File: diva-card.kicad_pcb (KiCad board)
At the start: 2 copper layers, 85.4 x 53.7 mm, 88 parts, among them J1 Conn_02x05_Odd_Even, J2 USB_C_Receptacle_USB2.0, J3 Conn_02x21_Odd_Even, SW1 SW_Push, SW2 SW_Push, U1 AP2112K-3.3, U2 ATECC608A-SSHDA, U3 W25Q128JVS, U4 RP2040, Y1 Crystal_GND24

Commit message: Adding test gerber and bom
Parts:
- D1: value RED -> EMERALD
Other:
- board text added: "0"
- board text added: "40"
- board text added: "RGB Matrix"
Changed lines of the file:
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@@
     (property "Sheetfile" "connectors.kicad_sch")
     (property "Sheetname" "connectors")
+    (attr exclude_from_bom)
     (fp_text reference "J3" (at 0 -26.9 unlocked) (layer "F.Fab")
       (effects (font (size 1 1) (thickness 0.15)))
@@
       (effects (font (size 1 1) (thickness 0.15)))
     )
-    (fp_text value "RED" (at 0 1.17) (layer "F.Fab")
+    (fp_text value "EMERALD" (at 0 1.17) (layer "F.Fab")
       (effects (font (size 1 1) (thickness 0.15)))
     )
@@
     (fp_line (start -2.5 -3.5) (end 3.5 -3.5) (layer "F.Fab") (width 0.1))
     (fp_line (start -3.5 -2.5) (end -2.5 -3.5) (layer "F.Fab") (width 0.1))
-    (pad "" smd roundrect (at -0.6375 0.6375 180) (size 1.084435 1.084435) (layers "F.Paste") (roundrect_rratio 0.230535))
-    (pad "" smd roundrect (at 0.6375 -0.6375 180) (size 1.084435 1.084435) (layers "F.Paste") (roundrect_rratio 0.230535))
-    (pad "" smd roundrect (at -0.6375 -0.6375 180) (size 1.084435 1.084435) (layers "F.Paste") (roundrect_rratio 0.230535))
-    (pad "" smd roundrect (at 0.6375 0.6375 180) (size 1.084435 1.084435) (layers "F.Paste") (roundrect_rratio 0.230535))
+    (pad "" smd roundrect (at -0.6375 0.6375 180) (size 1.084435 1.084435) (layers "F.Paste") (roundrect_rratio 0.2305347946))
+    (pad "" smd roundrect (at 0.6375 -0.6375 180) (size 1.084435 1.084435) (layers "F.Paste") (roundrect_rratio 0.2305347946))
+    (pad "" smd roundrect (at -0.6375 -0.6375 180) (size 1.084435 1.084435) (layers "F.Paste") (roundrect_rratio 0.2305347946))
+    (pad "" smd roundrect (at 0.6375 0.6375 180) (size 1.084435 1.084435) (layers "F.Paste") (roundrect_rratio 0.2305347946))
     (pad "1" smd roundrect (at -3.4375 -2.6 180) (size 0.875 0.2) (layers "F.Cu" "F.Paste" "F.Mask") (roundrect_rratio 0.25)
       (net 2 "+3V3") (pinfunction "IOVDD") (pintype "power_in"))
@@
     (property "Sheetfile" "connectors.kicad_sch")
     (property "Sheetname" "connectors")
-    (attr exclude_from_pos_files)
+    (attr exclude_from_pos_files exclude_from_bom)
     (fp_text reference "J1" (at 0 -2.6) (layer "F.Fab")
       (effects (font (size 1 1) (thickness 0.15)))
@@
     (property "Sheetfile" "peripherals.kicad_sch")
     (property "Sheetname" "peripherals")
-    (attr smd)
+    (attr smd exclude_from_bom)
     (fp_text reference "R3" (at -0.02 1.65 180) (layer "F.SilkS")
       (effects (font (size 1 1) (thickness 0.15)))
@@
   (gr_line (start 99.744 97.13) (end 100.76 96.114) (layer "F.SilkS") (width 0.15))
   (gr_line (start 95.32 97.13) (end 99.744 97.13) (layer "F.SilkS") (width 0.15))
+  (gr_line (start 109.45 105.333) (end 109.45 110.8) (layer "F.SilkS") (width 0.15))
   (gr_line (start 72.459 90.209) (end 73.475 91.225) (layer "F.SilkS") (width 0.15))
   (gr_line (start 78.876 97.875) (end 77.86 98.891) (layer "F.SilkS") (width 0.15))
@@
   (gr_line (start 137.057 81.274) (end 136.041 82.29) (layer "F.SilkS") (width 0.15))
   (gr_line (start 137.057 98.842) (end 136.041 99.858) (layer "F.SilkS") (width 0.15))
+  (gr_line (start 110.466 104.317) (end 109.45 105.333) (layer "F.SilkS") (width 0.15))
   (gr_line (start 86.534 78.534) (end 80.143 78.534) (layer "F.SilkS") (width 0.15))
   (gr_line (start 136.041 88.386) (end 136.041 91.434) (layer "F.SilkS") (width 0.15))
@@
   (gr_line (start 102.884 100.284) (end 103.9 101.3) (layer "F.SilkS") (width 0.15))
   (gr_line (start 136.041 82.29) (end 136.041 85.338) (layer "F.SilkS") (width 0.15))
-  (gr_line (start 107.232 74.692) (end 102.808 74.692) (layer "F.SilkS") (width 0.15))
+  (gr_line (start 109.049 74.8) (end 104.625 74.8) (layer "F.SilkS") (width 0.15))
   (gr_line (start 136.041 99.858) (end 136.041 102.906) (layer "F.SilkS") (width 0.15))
   (gr_line (start 136.041 111.754) (end 137.057 112.77) (layer "F.SilkS") (width 0.15))
@@
   (gr_line (start 83.3 97.875) (end 78.876 97.875) (layer "F.SilkS") (width 0.15))
   (gr_line (start 137.057 62.478) (end 136.041 63.494) (layer "F.SilkS") (width 0.15))
-  (gr_line (start 102.808 74.692) (end 101.792 75.708) (layer "F.SilkS") (width 0.15))
+  (gr_line (start 104.625 74.8) (end 103.609 75.816) (layer "F.SilkS") (width 0.15))
   (gr_line (start 72.459 88.084) (end 72.459 90.209) (layer "F.SilkS") (width 0.15))
   (gr_line locked (start 63.6 113.65) (end 63.6 61.35) (layer "Edge.Cuts") (width 0.1))
@@
     (effects (font (size 1 1) (thickness 0.15)))
   )
+  (gr_text "40" (at 128.025 69.875 90) (layer "F.SilkS")
+    (effects (font (size 1 1) (thickness 0.15)))
+  )
   (gr_text "SWD" (at 69.8 62.95) (layer "F.SilkS")
     (effects (font (size 1 1) (thickness 0.15)))
@@
     (effects (font (size 1 1) (thickness 0.15)))
   )
+  (gr_text "0" (at 109.85 102.375 90) (layer "F.SilkS")
+    (effects (font (size 1 1) (thickness 0.15)))
+  )
   (gr_text "V1.0" (at 70.5612 97.8408 90) (layer "F.SilkS")
     (effects (font (size 1 1) (thickness 0.25)))
@@
     (effects (font (size 1 1) (thickness 0.15)))
   )
-  (gr_text "Crypto" (at 105.04 73.66) (layer "F.SilkS")
+  (gr_text "Crypto" (at 106.857 73.768) (layer "F.SilkS")
     (effects (font (size 1 1) (thickness 0.15)))
   )
@@
     (effects (font (size 1 1) (thickness 0.15)))
   )
+  (gr_text "RGB Matrix" (at 108.75 108.175 90) (layer "F.SilkS")
+    (effects (font (size 1 1) (thickness 0.15)))
+  )
   (gr_text "DIVA CARD" (at 68.5612 97.8408 90) (layer "F.SilkS")
     (effects (font (size 1 1) (thickness 0.25)))
   )
-  (segment (start 92.5276 71.1876) (end 92.47 71.13) (width 0.5) (layer "F.Cu") (net 1))
   (segment (start 97.73 87.11) (end 98.62 87.11) (width 0.5) (layer "F.Cu") (net 1))
   (segment (start 120.393 104.768) (end 121.299 104.768) (width 0.3) (layer "F.Cu") (net 1))
@@
   (segment (start 114.963001 96.620242) (end 114.963001 96.018001) (width 0.3) (layer "F.Cu") (net 1))
   (segment (start 125.463001 91.977385) (end 125.463001 91.368001) (width 0.3) (layer "F.Cu") (net 1))
-  (segment (start 93.916 71.1876) (end 92.5276 71.1876) (width 0.5) (layer "F.Cu") (net 1))
   (segment (start 111.463 91.977385) (end 111.463 93.068) (width 0.3) (layer "F.Cu") (net 1))
   (segment (start 86 90.25) (end 86 88.095) (width 0.5) (layer "F.Cu") (net 1))
@@
   (segment (start 114.963001 101.2631) (end 114.963001 100.668001) (width 0.3) (layer "F.Cu") (net 1))
   (segment (start 79.3496 99.2704) (end 79.35 99.27) (width 0.5) (layer "F.Cu") (net 1))
+  (segment (start 92.475 71.2) (end 92.4874 71.1876) (width 0.5) (layer "F.Cu") (net 1))
   (segment (start 121.963001 87.334528) (end 121.963001 86.668501) (width 0.3) (layer "F.Cu") (net 1))
   (segment (start 118.463001 101.2631) (end 118.463001 100.668001) (width 0.3) (layer "F.Cu") (net 1))
@@
   (segment (start 125.463001 86.668001) (end 124.863 86.068) (width 0.3) (layer "F.Cu") (net 1))
   (segment (start 118.463001 72.783687) (end 117.872859 72.193545) (width 0.3) (layer "F.Cu") (net 1))
+  (segment (start 92.4874 71.1876) (end 93.916 71.1876) (width 0.5) (layer "F.Cu") (net 1))
   (segment (start 111.399976 97.704976) (end 111.413 97.718) (width 0.3) (layer "F.Cu") (net 1))
   (segment (start 114.963001 68.7631) (end 114.963 69.868) (width 0.3) (layer "F.Cu") (net 1))
@@
   (via (at 97.59 72.87) (size 0.7) (drill 0.3) (layers "F.Cu" "B.Cu") (net 1))
   (via (at 71.055659 67.4626) (size 0.7) (drill 0.3) (layers "F.Cu" "B.Cu") (net 1))
-  (via (at 92.47 71.13) (size 0.7) (drill 0.3) (layers "F.Cu" "B.Cu") (net 1))
+  (via (at 92.475 71.2) (size 0.7) (drill 0.3) (layers "F.Cu" "B.Cu") (net 1))
   (via (at 114.372859 86.093545) (size 0.7) (drill 0.3) (layers "F.Cu" "B.Cu") (net 1))
   (via (at 117.863 81.518) (size 0.7) (drill 0.3) (layers "F.Cu" "B.Cu") (net 1))

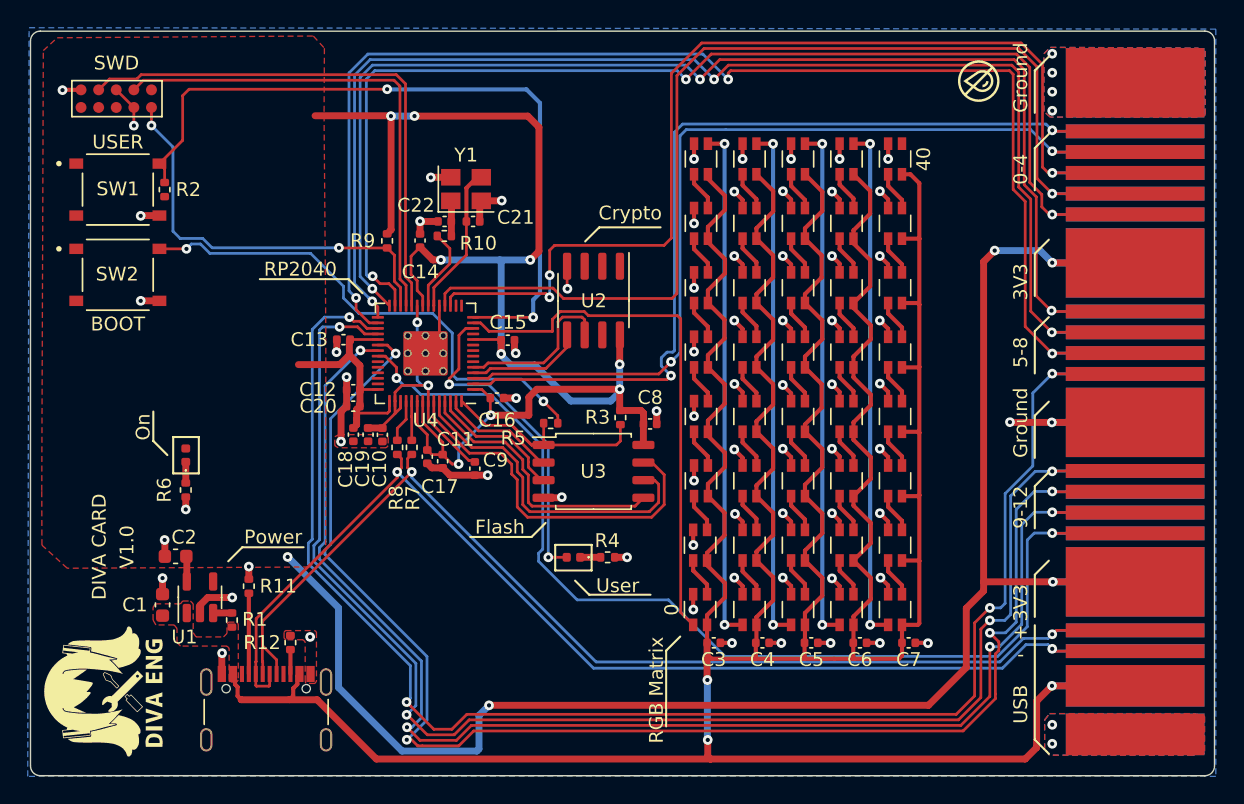
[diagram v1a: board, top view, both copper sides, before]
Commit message: updating footprints to udfn
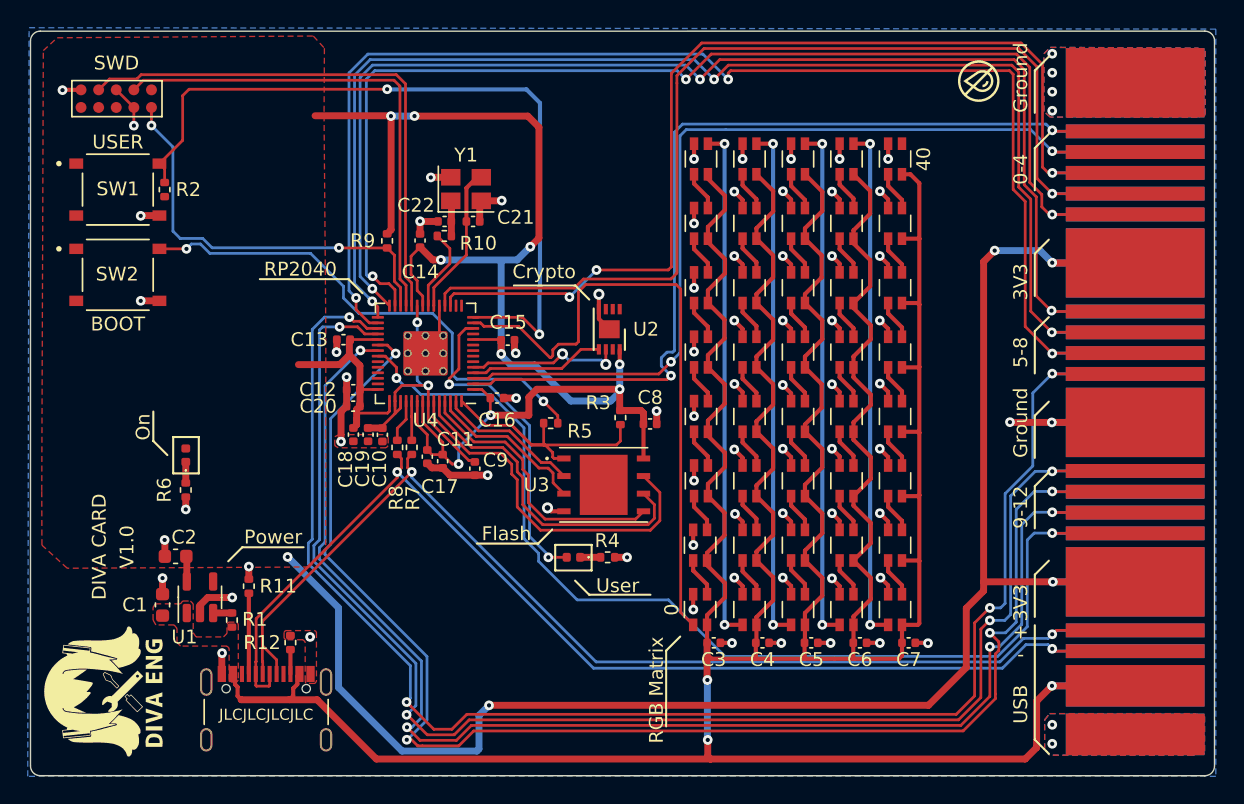
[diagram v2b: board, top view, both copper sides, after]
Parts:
- R5: value 1k -> 10k
- U2: value ATECC608A-SSHDA -> ATECC608A-MAHDA; footprint Package_SO:SOIC-8_3.9x4.9mm_P1.27mm -> Package_DFN_QFN:DFN-8-1EP_3x2mm_P0.5mm_EP1.3x1.5mm
- U3: value W25Q128JVS -> W25Q128XXX; footprint Package_SO:SOIC-8_5.23x5.23mm_P1.27mm -> Diva-Card:W25Q128JVPIQ TR
- moved U2 2.36 mm to (105.3, 82.2)
- moved U3 1.22 mm to (104.9, 93.4)
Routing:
- net /LED_DI: track 39.0 -> 45.3 mm
- net /microcontroller/~{QSPI_CS}: track 18.5 -> 20.6 mm
- net /~{USER_SW0}: track 53.5 -> 55.5 mm
- net /microcontroller/QSPI_SIO1: track 8.47 -> 10.3 mm
- net /microcontroller/QSPI_SIO2: track 9.90 -> 11.8 mm
- net /connectors/USER_IO_3: track 82.8 -> 81.4 mm
- net /I2C0_SDA: track 8.43 -> 9.77 mm
- net GND: track 114.9 -> 116.1 mm
- net /connectors/USER_IO_2: track 81.0 -> 80.2 mm
- net +3V3: track 252.1 -> 251.5 mm
- net /I2C0_SCL: track 11.9 -> 11.4 mm, vias 0 -> 2
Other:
- board text added: "JLCJLCJLCJLC"

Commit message: Adding schematic pdf
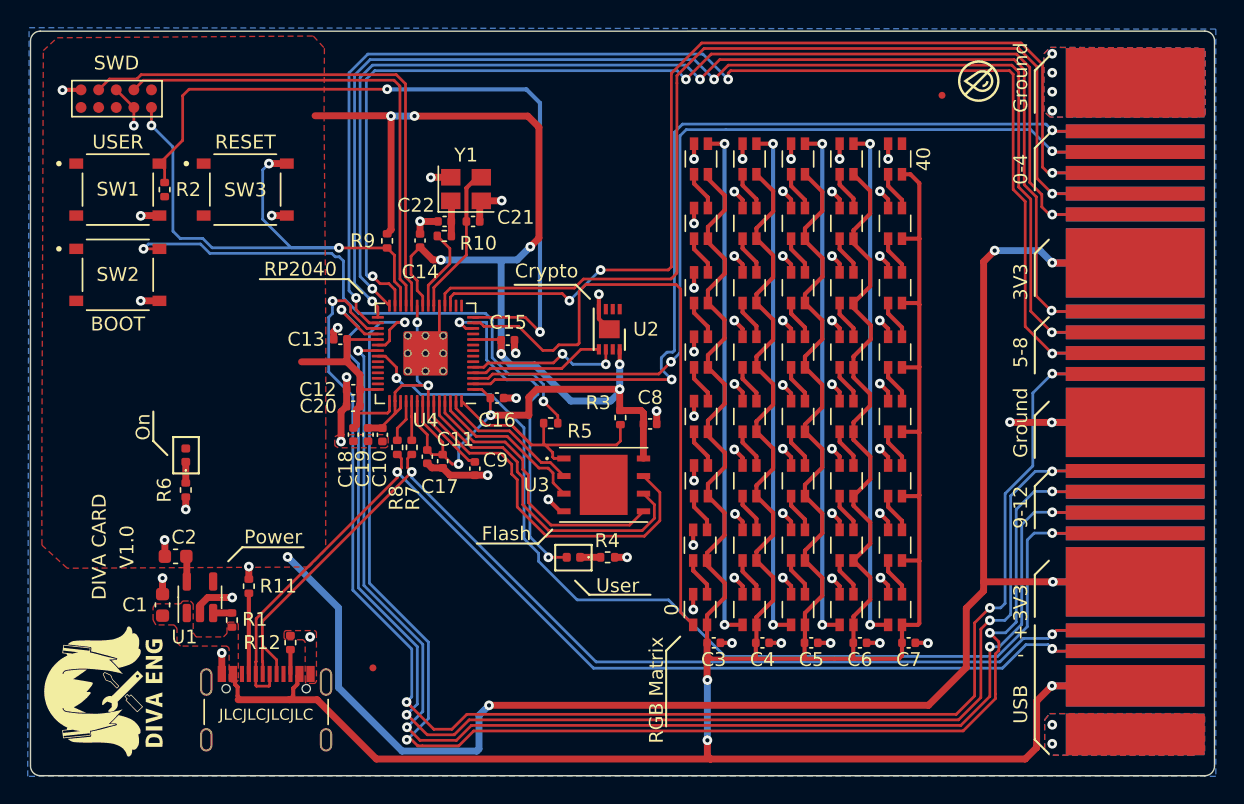
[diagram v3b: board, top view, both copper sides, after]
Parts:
- added FID1: Fiducial, Fiducial:Fiducial_0.5mm_Mask1mm, F.Cu at (88.3, 106.6)
- added FID2: Fiducial, Fiducial:Fiducial_0.5mm_Mask1mm, F.Cu at (129.3, 65.3)
- added SW3: RESET, Diva-Card:SW_TS-1187A-B-A-B, F.Cu at (79.1, 72.1)
- C21, C22: value 22p -> 33p
- R5: value 10k -> 1k
- SW1: value SW_Push -> USER
- SW2: value SW_Push -> BOOTSEL
- Y1: value Crystal_GND24 -> X322512MSB4SI
- moved C13 0.23 mm to (86.0, 82.9)
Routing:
- net /connectors/~{RESET}: track 30.1 -> 41.9 mm, vias 2 -> 3
- net /peripherals/~{USB_BOOT}: track 36.8 -> 40.7 mm
- net /connectors/USER_IO_10: track 110.0 -> 112.5 mm
- net /connectors/USER_IO_11: track 105.4 -> 103.0 mm
- net GND: track 116.1 -> 117.4 mm, vias 77 -> 78
- net /USER_LED: track 23.5 -> 24.8 mm
- net /microcontroller/~{QSPI_CS}: track 20.6 -> 19.6 mm
- net /LED_DI: track 45.3 -> 44.7 mm
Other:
- board text added: "RESET"

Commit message: design flaw fix
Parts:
- added C23: 1u, Capacitor_SMD:C_0402_1005Metric, F.Cu at (82.5, 72.0)
- added C24: 1u, Capacitor_SMD:C_0402_1005Metric, F.Cu at (101.8, 82.3)
- added C25: 1u, Capacitor_SMD:C_0402_1005Metric, F.Cu at (104.5, 89.0)
- R10: value 1k -> DNF
- R3: value DNF -> 10k
- moved FID1 4.17 mm to (88.6, 110.7)
- moved FID2 0.06 mm to (129.3, 65.3)
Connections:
- J3 pad 35: /connectors/USB_D+ -> unconnected-(J3-Pad35)
- J3 pad 36: /connectors/USB_D+ -> unconnected-(J3-Pad36)
- J3 pad 37: /connectors/USB_D- -> unconnected-(J3-Pad37)
- J3 pad 38: /connectors/USB_D- -> unconnected-(J3-Pad38)
- U4 pad 44: +1V1 -> +3V3
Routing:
- net +3V3: track 251.1 -> 108.6 mm, vias 14 -> 27
- net +5V: track 315.9 -> 215.0 mm
- net /connectors/USB_D-: track 89.0 -> 22.8 mm, vias 2 -> 0
- net /connectors/USB_D+: track 88.2 -> 22.7 mm, vias 2 -> 0
- net /connectors/USER_IO_12: track 82.4 -> 104.8 mm, vias 2 -> 4
- net GND: track 117.4 -> 107.2 mm, vias 78 -> 82
- net /connectors/USER_IO_10: track 112.5 -> 108.0 mm
- net /connectors/USER_IO_9: track 110.7 -> 113.8 mm
- net /connectors/~{RESET}: track 41.9 -> 43.5 mm
- net /connectors/USER_IO_1: track 71.0 -> 72.3 mm
- net +1V1: track 20.6 -> 19.3 mm
- net /microcontroller/~{QSPI_CS}: track 19.6 -> 20.7 mm
- net /~{USER_SW0}: track 55.3 -> 56.2 mm
- net /microcontroller/XOUT: track 6.05 -> 6.60 mm
- net /connectors/USER_IO_11: track 103.0 -> 102.7 mm, vias 4 -> 2
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- added copper zone on B.Cu, net +3V3
- added copper zone on B.Cu, net +5V
